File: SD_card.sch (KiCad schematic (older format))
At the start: 1 part

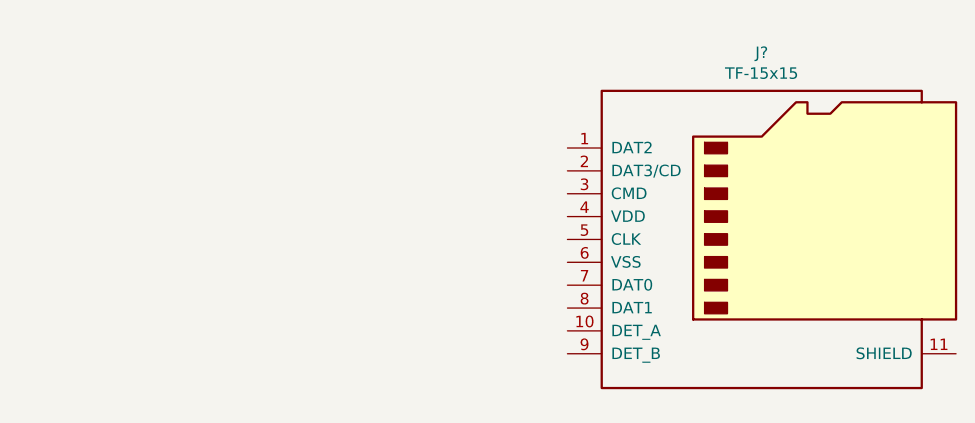
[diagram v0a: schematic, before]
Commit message: Connect SD card
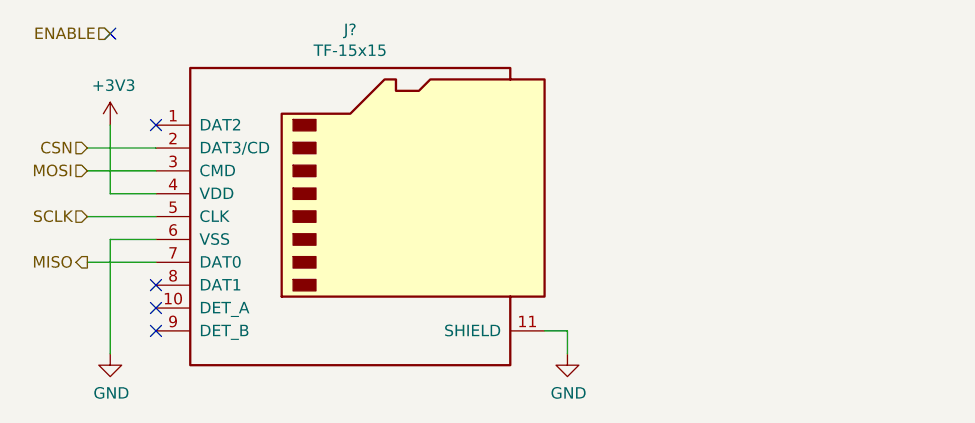
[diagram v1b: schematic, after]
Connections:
- net GND: now reaches J?.11 (SHIELD)
- net GND: now also J?.6 (VSS)
- net CSN: now reaches J?.2 (DAT3/CD)
- net MOSI: now reaches J?.3 (CMD)
- net +3V3: now reaches J?.4 (VDD)
- net SCLK: now reaches J?.5 (CLK)
- net MISO: now reaches J?.7 (DAT0)
- no-connect marks 0 -> 5
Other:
- moved on the sheet: J?
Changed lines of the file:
@@
 L Connector:Micro_SD_Card_Det J?
 U 1 1 60B61966
-P 7900 4000
-F 0 "J?" H 7850 4817 50  0000 C CNN
-F 1 "TF-15x15" H 7850 4726 50  0000 C CNN
-F 2 "" H 9950 4700 50  0001 C CNN
-F 3 "https://datasheet.lcsc.com/szlcsc/2009111836_SOFNG-TF-15x15_C111196.pdf" H 7900 4100 50  0001 C CNN
-F 4 "https://lcsc.com/product-detail/Card-Sockets-Connectors_SOFNG-TF-15x15_C111196.html/?href=jlc-SMT" H 7900 4000 50  0001 C CNN "LCSC"
-	1    7900 4000
+P 6100 3900
+F 0 "J?" H 6050 4717 50  0000 C CNN
+F 1 "TF-15x15" H 6050 4626 50  0000 C CNN
+F 2 "" H 8150 4600 50  0001 C CNN
+F 3 "https://datasheet.lcsc.com/szlcsc/2009111836_SOFNG-TF-15x15_C111196.pdf" H 6100 4000 50  0001 C CNN
+F 4 "https://lcsc.com/product-detail/Card-Sockets-Connectors_SOFNG-TF-15x15_C111196.html/?href=jlc-SMT" H 6100 3900 50  0001 C CNN "LCSC"
+	1    6100 3900
 	1    0    0    -1
 $EndComp
+Text HLabel 4900 3900 0    50   Input ~ 0
+SCLK
+Text HLabel 4900 4100 0    50   Output ~ 0
+MISO
+Text HLabel 4900 3700 0    50   Input ~ 0
+MOSI
+Text HLabel 4900 3600 0    50   Input ~ 0
+CSN
+Text HLabel 5000 3100 0    50   Input ~ 0
+ENABLE
+Wire Wire Line
+	4900 4100 5200 4100
+Wire Wire Line
+	4900 3700 5200 3700
+Wire Wire Line
+	4900 3600 5200 3600
+Wire Wire Line
+	5200 3800 5000 3800
+Wire Wire Line
+	5000 3800 5000 3500
+Wire Wire Line
+	5200 4000 5000 4000
+$Comp
+L power:GND #PWR?
+U 1 1 60A80F45
+P 5000 4500
+F 0 "#PWR?" H 5000 4250 50  0001 C CNN
+F 1 "GND" H 5005 4327 50  0000 C CNN
+F 2 "" H 5000 4500 50  0001 C CNN
+F 3 "" H 5000 4500 50  0001 C CNN
+	1    5000 4500
+	1    0    0    -1
+$EndComp
+$Comp
+L power:+3V3 #PWR?
+U 1 1 60A815FB
+P 5000 3500
+F 0 "#PWR?" H 5000 3350 50  0001 C CNN
+F 1 "+3V3" H 5015 3673 50  0000 C CNN
+F 2 "" H 5000 3500 50  0001 C CNN
+F 3 "" H 5000 3500 50  0001 C CNN
+	1    5000 3500
+	1    0    0    -1
+$EndComp
+$Comp
+L power:GND #PWR?
+U 1 1 60A81A13
+P 7000 4500
+F 0 "#PWR?" H 7000 4250 50  0001 C CNN
+F 1 "GND" H 7005 4327 50  0000 C CNN
+F 2 "" H 7000 4500 50  0001 C CNN
+F 3 "" H 7000 4500 50  0001 C CNN
+	1    7000 4500
+	1    0    0    -1
+$EndComp
+Wire Wire Line
+	6900 4400 7000 4400
+Wire Wire Line
+	7000 4400 7000 4500
+NoConn ~ 5000 3100
+NoConn ~ 5200 3500
+NoConn ~ 5200 4200
+NoConn ~ 5200 4300
+NoConn ~ 5200 4400
+Wire Wire Line
+	5000 4000 5000 4500
+Wire Wire Line
+	4900 3900 5200 3900
 $EndSCHEMATC

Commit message: Change BME280 out for connector
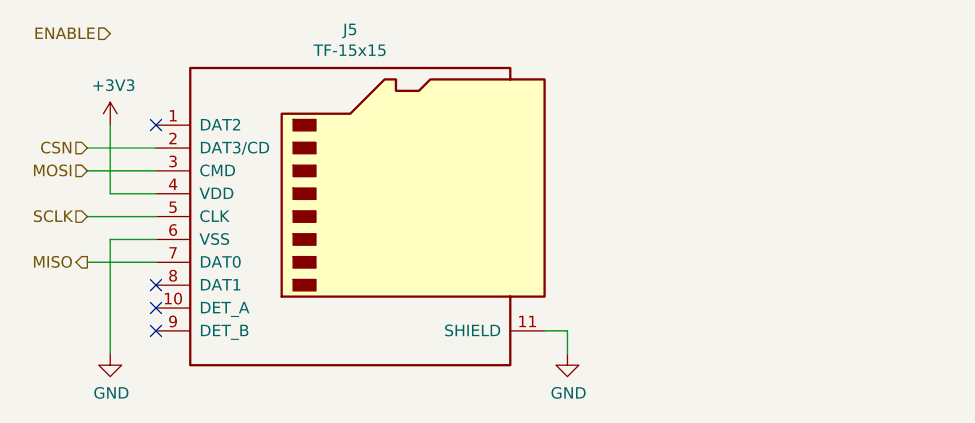
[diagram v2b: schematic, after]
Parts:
- gave numbers to parts that had none: 1
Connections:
- no-connect marks 5 -> 4
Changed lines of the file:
@@
 $EndDescr
 $Comp
-L Connector:Micro_SD_Card_Det J?
+L Connector:Micro_SD_Card_Det J5
 U 1 1 60B61966
 P 6100 3900
-F 0 "J?" H 6050 4717 50  0000 C CNN
+F 0 "J5" H 6050 4717 50  0000 C CNN
 F 1 "TF-15x15" H 6050 4626 50  0000 C CNN
 F 2 "" H 8150 4600 50  0001 C CNN
@@
 Text HLabel 4900 3600 0    50   Input ~ 0
 CSN
-Text HLabel 5000 3100 0    50   Input ~ 0
-ENABLE
 Wire Wire Line
 	4900 4100 5200 4100
@@
 	5200 4000 5000 4000
 $Comp
-L power:GND #PWR?
+L power:GND #PWR016
 U 1 1 60A80F45
 P 5000 4500
-F 0 "#PWR?" H 5000 4250 50  0001 C CNN
+F 0 "#PWR016" H 5000 4250 50  0001 C CNN
 F 1 "GND" H 5005 4327 50  0000 C CNN
 F 2 "" H 5000 4500 50  0001 C CNN
@@
 $EndComp
 $Comp
-L power:+3V3 #PWR?
+L power:+3V3 #PWR015
 U 1 1 60A815FB
 P 5000 3500
-F 0 "#PWR?" H 5000 3350 50  0001 C CNN
+F 0 "#PWR015" H 5000 3350 50  0001 C CNN
 F 1 "+3V3" H 5015 3673 50  0000 C CNN
 F 2 "" H 5000 3500 50  0001 C CNN
@@
 $EndComp
 $Comp
-L power:GND #PWR?
+L power:GND #PWR017
 U 1 1 60A81A13
 P 7000 4500
-F 0 "#PWR?" H 7000 4250 50  0001 C CNN
+F 0 "#PWR017" H 7000 4250 50  0001 C CNN
 F 1 "GND" H 7005 4327 50  0000 C CNN
 F 2 "" H 7000 4500 50  0001 C CNN
@@
 Wire Wire Line
 	7000 4400 7000 4500
-NoConn ~ 5000 3100
 NoConn ~ 5200 3500
 NoConn ~ 5200 4200
@@
 Wire Wire Line
 	4900 3900 5200 3900
+Text HLabel 5000 3100 0    50   Input ~ 0
+ENABLE
 $EndSCHEMATC

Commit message: Begin assigning footprints
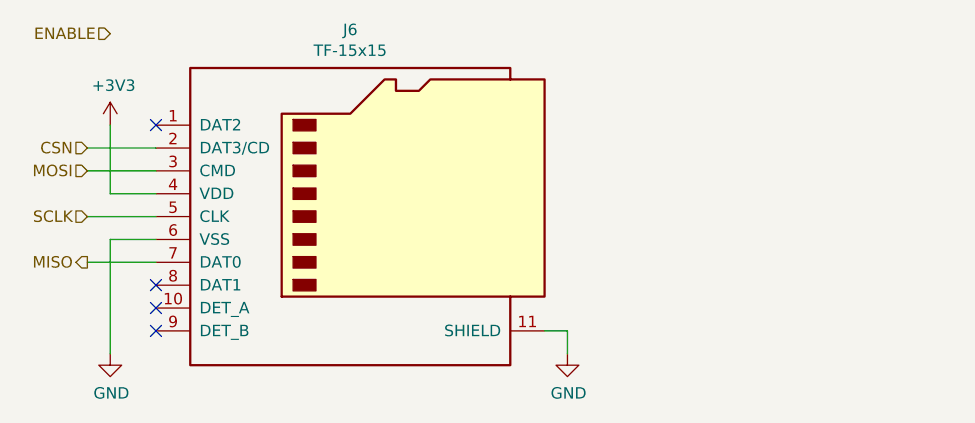
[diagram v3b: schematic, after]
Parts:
- J6: renamed from J5; LCSC https://lcsc.com/product-detail/Card-Sockets-Connectors_SOF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 -> C111196
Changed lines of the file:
@@
 $EndDescr
 $Comp
-L Connector:Micro_SD_Card_Det J5
+L Connector:Micro_SD_Card_Det J6
 U 1 1 60B61966
 P 6100 3900
-F 0 "J5" H 6050 4717 50  0000 C CNN
+F 0 "J6" H 6050 4717 50  0000 C CNN
 F 1 "TF-15x15" H 6050 4626 50  0000 C CNN
 F 2 "" H 8150 4600 50  0001 C CNN
 F 3 "https://datasheet.lcsc.com/szlcsc/2009111836_SOFNG-TF-15x15_C111196.pdf" H 6100 4000 50  0001 C CNN
-F 4 "https://lcsc.com/product-detail/Card-Sockets-Connectors_SOFNG-TF-15x15_C111196.html/?href=jlc-SMT" H 6100 3900 50  0001 C CNN "LCSC"
+F 4 "C111196" H 6100 3900 50  0001 C CNN "LCSC"
 	1    6100 3900
 	1    0    0    -1
@@
 	5200 4000 5000 4000
 $Comp
-L power:GND #PWR016
+L power:GND #PWR014
 U 1 1 60A80F45
 P 5000 4500
-F 0 "#PWR016" H 5000 4250 50  0001 C CNN
+F 0 "#PWR014" H 5000 4250 50  0001 C CNN
 F 1 "GND" H 5005 4327 50  0000 C CNN
 F 2 "" H 5000 4500 50  0001 C CNN
@@
 $EndComp
 $Comp
-L power:+3V3 #PWR015
+L power:+3V3 #PWR013
 U 1 1 60A815FB
 P 5000 3500
-F 0 "#PWR015" H 5000 3350 50  0001 C CNN
+F 0 "#PWR013" H 5000 3350 50  0001 C CNN
 F 1 "+3V3" H 5015 3673 50  0000 C CNN
 F 2 "" H 5000 3500 50  0001 C CNN
@@
 $EndComp
 $Comp
-L power:GND #PWR017
+L power:GND #PWR015
 U 1 1 60A81A13
 P 7000 4500
-F 0 "#PWR017" H 7000 4250 50  0001 C CNN
+F 0 "#PWR015" H 7000 4250 50  0001 C CNN
 F 1 "GND" H 7005 4327 50  0000 C CNN
 F 2 "" H 7000 4500 50  0001 C CNN

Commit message: Finish attaching footprints for revision 1
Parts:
- J6: footprint (none) -> co2_sensor_node:TF-15x15
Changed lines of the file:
@@
 F 0 "J6" H 6050 4717 50  0000 C CNN
 F 1 "TF-15x15" H 6050 4626 50  0000 C CNN
-F 2 "" H 8150 4600 50  0001 C CNN
+F 2 "co2_sensor_node:TF-15x15" H 8150 4600 50  0001 C CNN
 F 3 "https://datasheet.lcsc.com/szlcsc/2009111836_SOFNG-TF-15x15_C111196.pdf" H 6100 4000 50  0001 C CNN
 F 4 "C111196" H 6100 3900 50  0001 C CNN "LCSC"

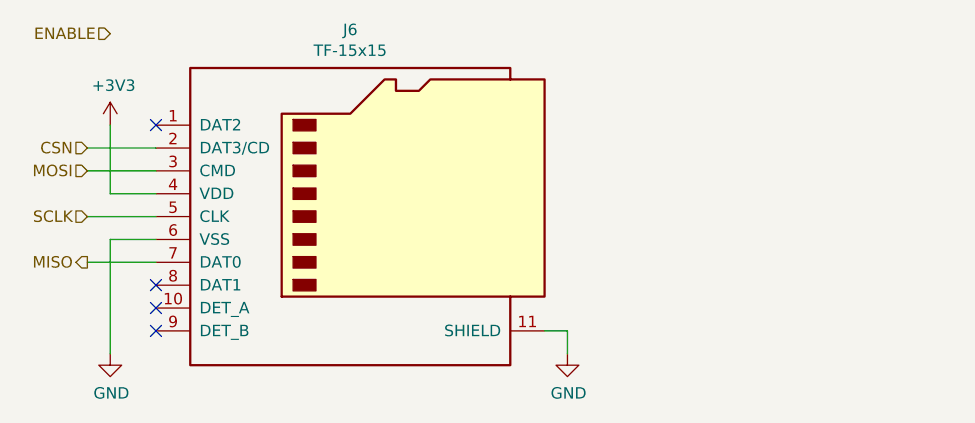
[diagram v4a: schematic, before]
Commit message: First cut at layout
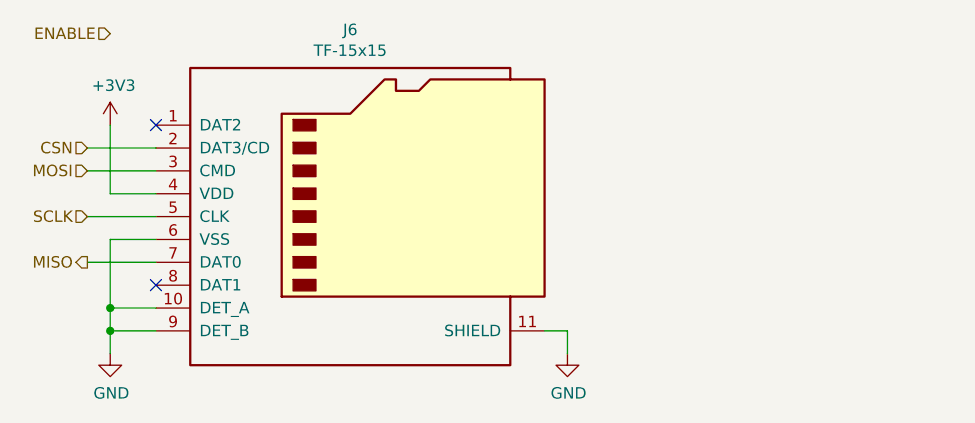
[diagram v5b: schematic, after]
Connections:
- net GND: now also J6.10 (DET_A), J6.9 (DET_B)
- no-connect marks 4 -> 2
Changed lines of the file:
@@
 NoConn ~ 5200 3500
 NoConn ~ 5200 4200
-NoConn ~ 5200 4300
-NoConn ~ 5200 4400
 Wire Wire Line
-	5000 4000 5000 4500
+	5000 4000 5000 4300
 Wire Wire Line
 	4900 3900 5200 3900
 Text HLabel 5000 3100 0    50   Input ~ 0
 ENABLE
+Wire Wire Line
+	5200 4300 5000 4300
+Connection ~ 5000 4300
+Wire Wire Line
+	5000 4300 5000 4400
+Wire Wire Line
+	5200 4400 5000 4400
+Connection ~ 5000 4400
+Wire Wire Line
+	5000 4400 5000 4500
 $EndSCHEMATC

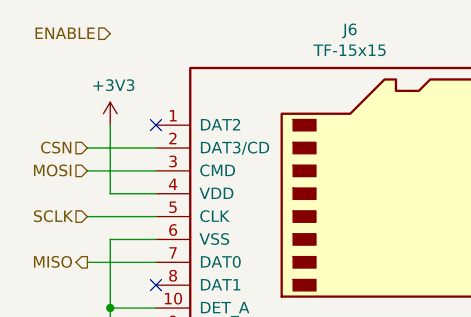
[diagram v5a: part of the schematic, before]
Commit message: Start changing design for long term chambers
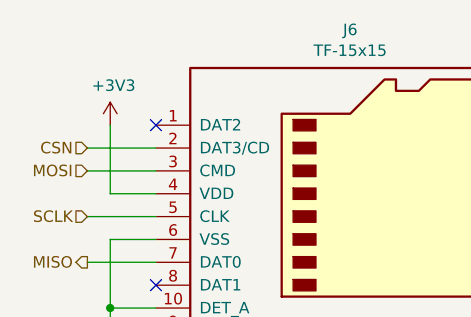
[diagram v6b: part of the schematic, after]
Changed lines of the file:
@@
 Wire Wire Line
 	4900 3900 5200 3900
-Text HLabel 5000 3100 0    50   Input ~ 0
-ENABLE
 Wire Wire Line
 	5200 4300 5000 4300
